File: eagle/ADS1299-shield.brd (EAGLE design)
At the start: 101.6 x 53.3 mm, 133 parts, among them IC1 ADS1299IPAG, IC2 TPS72325DBVT, IC3 TPS73225DBVT, IC5 24AA256UID, IC6 TPS604XXDBV, IC7 OPA376DBV, IC8 OPA376DBV, IC9 TXS0102DCTR, J8 Electrode Connector, U2 TXB0108PWR, U3 TXB0108PWR

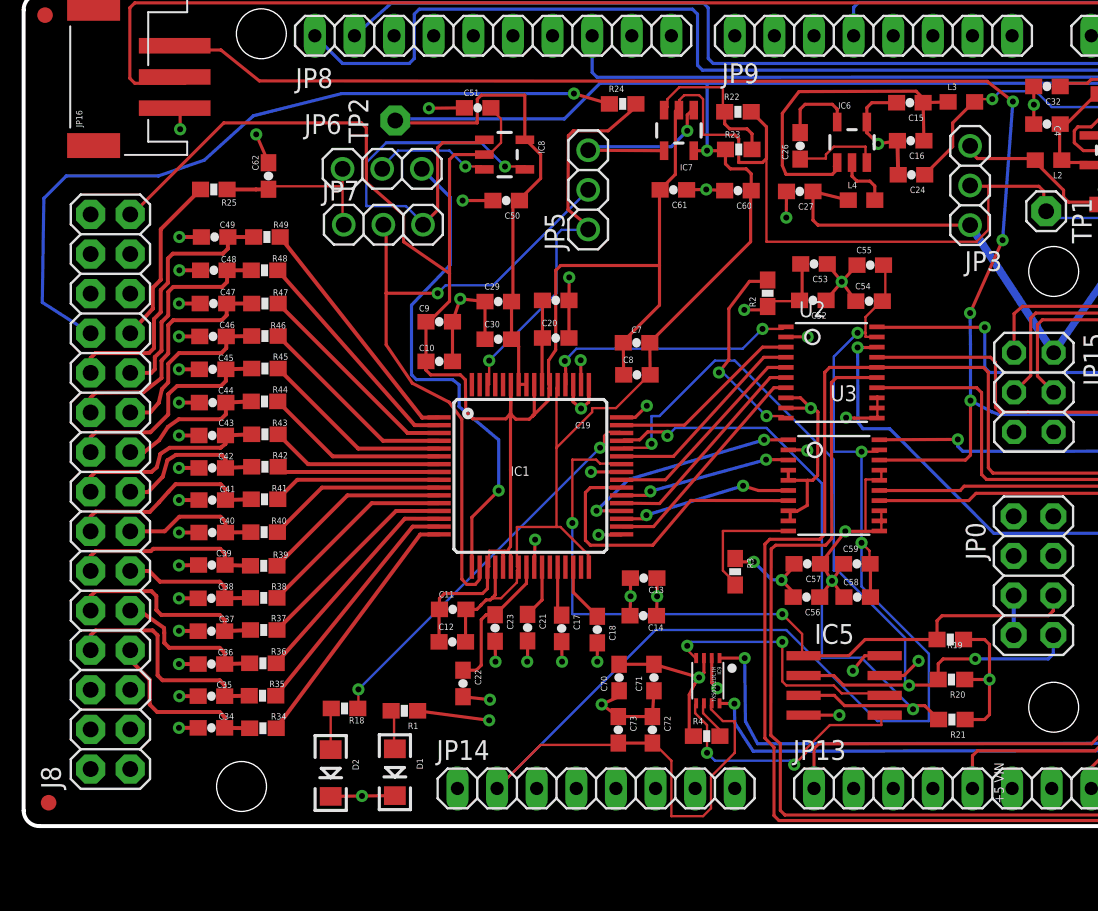
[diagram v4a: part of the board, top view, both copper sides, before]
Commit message: tom side of board is mitered and has polygons on T and V intersections
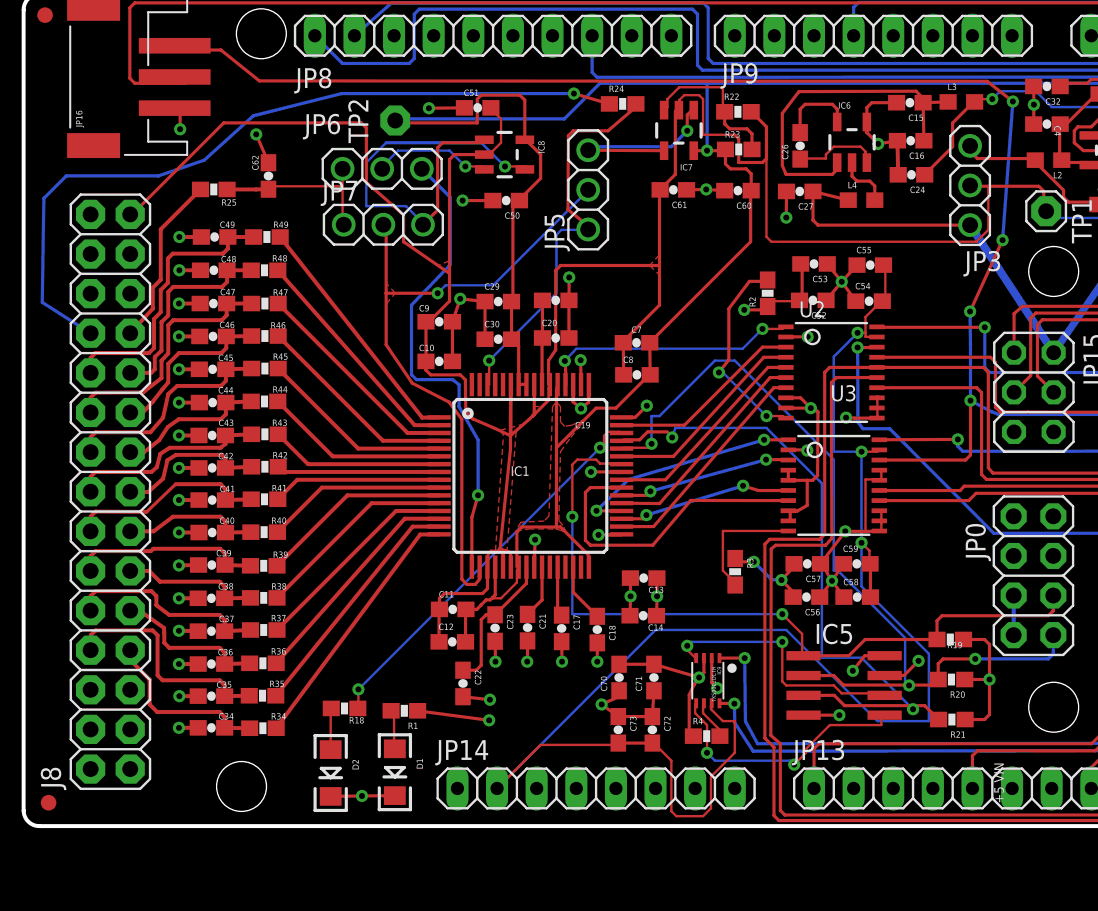
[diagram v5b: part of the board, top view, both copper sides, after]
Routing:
- net AGND: track 466.3 -> 492.9 mm
- net AVDD: track 184.9 -> 188.4 mm
- net SRB2: track 31.8 -> 30.3 mm
- net AVSS: track 163.8 -> 163.2 mm
- added copper zone on layer 1, net AVDD
- added copper zone on layer 1, net AVSS
- added copper zone on layer 1, net SRB1

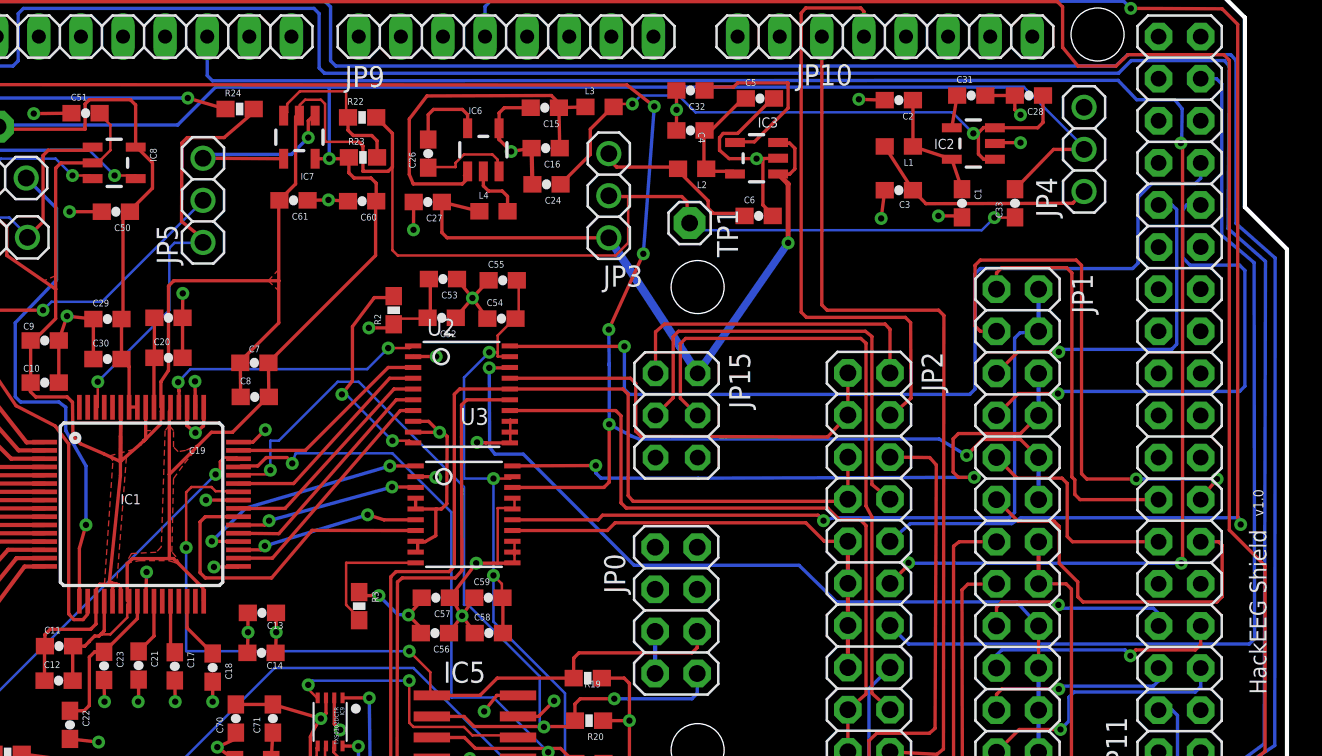
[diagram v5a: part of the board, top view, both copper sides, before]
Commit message: fixed DRC errors related to top-side polygons
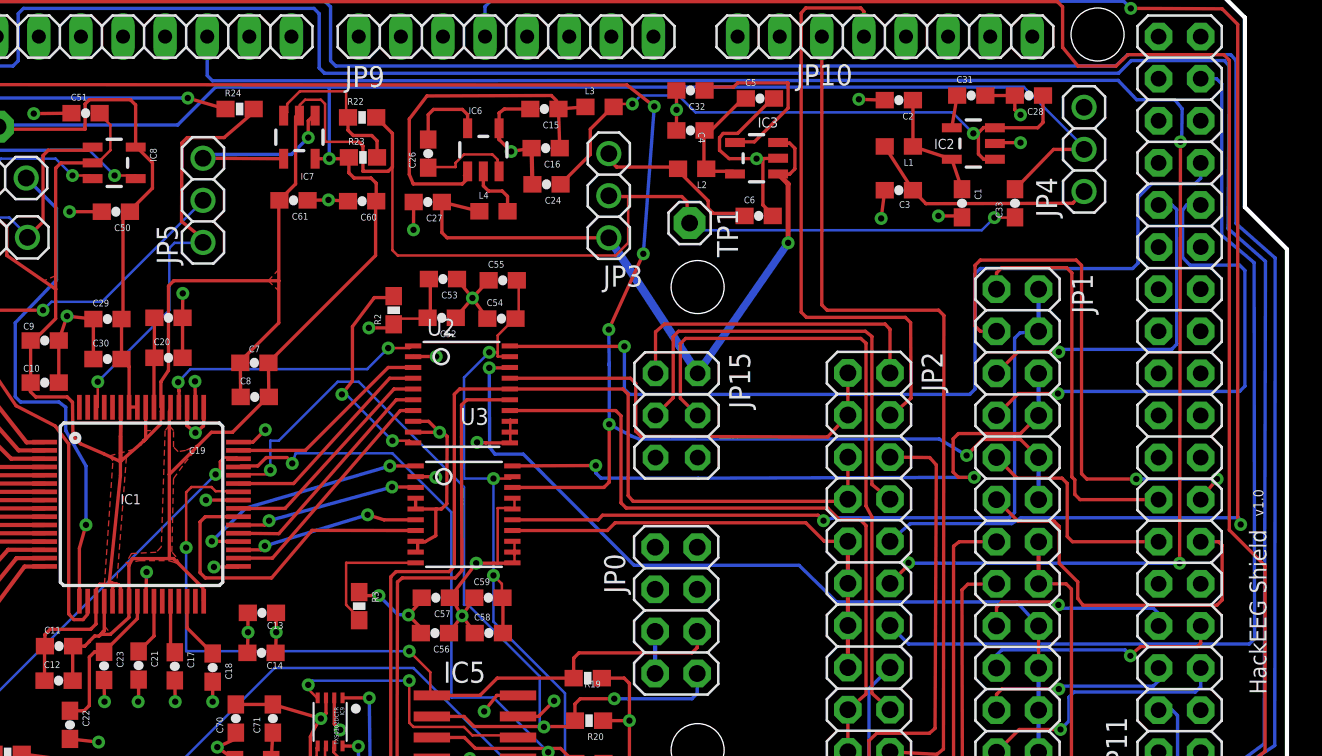
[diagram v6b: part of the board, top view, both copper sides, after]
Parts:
- moved C15 0.08 mm to (56.9, 46.4)
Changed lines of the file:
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@@
 <attribute name="VALUE" x="59.2328" y="45.4152" size="0.4064" layer="27" font="vector"/>
 </element>
-<element name="C15" library="SparkFun-Passives" package="0603-CAP" value="2.2uF" x="56.9468" y="46.5074" smashed="yes" rot="R180">
-<attribute name="NAME" x="57.8358" y="45.7454" size="0.4064" layer="25" font="vector" rot="R180"/>
-<attribute name="VALUE" x="57.9628" y="47.6504" size="0.4064" layer="27" font="vector" rot="R180"/>
+<element name="C15" library="SparkFun-Passives" package="0603-CAP" value="2.2uF" x="56.9214" y="46.4312" smashed="yes" rot="R180">
+<attribute name="NAME" x="57.8104" y="45.6692" size="0.4064" layer="25" font="vector" rot="R180"/>
+<attribute name="VALUE" x="57.9374" y="47.5742" size="0.4064" layer="27" font="vector" rot="R180"/>
 </element>
 <element name="C16" library="SparkFun-Passives" package="0603-CAP" value="10 uF" x="56.9976" y="44.069" smashed="yes" rot="R180">
@@
 <wire x1="80.5434" y1="39.8272" x2="77.2414" y2="39.8272" width="0.2032" layer="2"/>
 <wire x1="54.1884" y1="45.2675" x2="54.1884" y2="46.1899" width="0.2032" layer="1"/>
-<wire x1="54.1884" y1="46.1899" x2="54.5059" y2="46.5074" width="0.2032" layer="1"/>
-<wire x1="54.5059" y1="46.5074" x2="56.0968" y2="46.5074" width="0.2032" layer="1"/>
+<wire x1="54.1884" y1="46.1899" x2="54.5059" y2="46.4312" width="0.2032" layer="1"/>
+<wire x1="54.5059" y1="46.4312" x2="56.0714" y2="46.4312" width="0.2032" layer="1"/>
 <wire x1="55.3304" y1="9.779" x2="56.5658" y2="9.779" width="0.2032" layer="1"/>
 <wire x1="56.5658" y1="9.779" x2="57.5056" y2="10.7188" width="0.2032" layer="1"/>
@@
 <contactref element="C16" pad="1"/>
 <contactref element="IC6" pad="1"/>
-<wire x1="57.7968" y1="46.5074" x2="59.3988" y2="46.5582" width="0.2032" layer="1"/>
-<wire x1="57.7968" y1="46.5074" x2="57.8476" y2="44.069" width="0.2032" layer="1"/>
+<wire x1="57.7714" y1="46.4312" x2="59.3988" y2="46.5582" width="0.2032" layer="1"/>
+<wire x1="57.7714" y1="46.4312" x2="57.8476" y2="44.069" width="0.2032" layer="1"/>
 <wire x1="48.768" y1="45.8216" x2="48.768" y2="42.4815" width="0.2032" layer="1"/>
 <wire x1="48.768" y1="42.4815" x2="49.0093" y2="41.91" width="0.2032" layer="1"/>
@@
 <wire x1="57.3405" y1="47.244" x2="49.8348" y2="47.2186" width="0.2032" layer="1"/>
 <wire x1="52.07" y1="42.418" x2="52.2884" y2="42.6673" width="0.1524" layer="1"/>
-<wire x1="57.658" y1="46.736" x2="57.7968" y2="46.5074" width="0.1524" layer="1"/>
+<wire x1="57.658" y1="46.736" x2="57.7714" y2="46.4312" width="0.1524" layer="1"/>
 <wire x1="51.9709" y1="41.91" x2="52.2884" y2="42.2275" width="0.2032" layer="1"/>
 <wire x1="52.2884" y1="42.2275" x2="52.2884" y2="42.6673" width="0.2032" layer="1"/>
@@
 <contactref element="JP1" pad="14"/>
 <contactref element="JP11" pad="11"/>
-<wire x1="97.8154" y1="20.1041" x2="97.8154" y2="17.0053" width="0.2032" layer="1"/>
-<wire x1="97.8154" y1="17.0053" x2="97.4979" y2="16.6878" width="0.2032" layer="1"/>
-<wire x1="97.4979" y1="16.6878" x2="89.4207" y2="16.6878" width="0.2032" layer="1"/>
-<wire x1="89.4207" y1="16.6878" x2="89.1032" y2="17.0053" width="0.2032" layer="1"/>
-<wire x1="89.1032" y1="17.0053" x2="89.1032" y2="17.8943" width="0.2032" layer="1"/>
+<wire x1="97.8154" y1="20.1041" x2="97.8154" y2="16.8021" width="0.2032" layer="1"/>
+<wire x1="97.8154" y1="16.8021" x2="97.4979" y2="16.4846" width="0.2032" layer="1"/>
+<wire x1="97.4979" y1="16.4846" x2="89.4207" y2="16.4846" width="0.2032" layer="1"/>
+<wire x1="89.4207" y1="16.4846" x2="89.1032" y2="16.9037" width="0.2032" layer="1"/>
+<wire x1="89.1032" y1="16.9037" x2="89.1032" y2="17.8943" width="0.2032" layer="1"/>
 <wire x1="87.9856" y1="21.2471" x2="87.6681" y2="21.5646" width="0.2032" layer="1"/>
 <wire x1="87.6681" y1="21.5646" x2="85.4964" y2="21.5646" width="0.2032" layer="1"/>
@@
 <contactref element="JP1" pad="6"/>
 <contactref element="JP11" pad="7"/>
-<wire x1="96.52" y1="15.24" x2="96.52" y2="14.1097" width="0.2032" layer="1"/>
-<wire x1="96.52" y1="14.1097" x2="96.2025" y2="13.7922" width="0.2032" layer="1"/>
-<wire x1="96.2025" y1="13.7922" x2="92.5957" y2="13.7922" width="0.2032" layer="1"/>
-<wire x1="92.5957" y1="13.7922" x2="92.2782" y2="13.4747" width="0.2032" layer="1"/>
+<wire x1="96.52" y1="15.24" x2="96.52" y2="14.2113" width="0.2032" layer="1"/>
+<wire x1="96.52" y1="14.2113" x2="96.3041" y2="13.9954" width="0.2032" layer="1"/>
+<wire x1="96.3041" y1="13.9954" x2="92.9005" y2="13.9954" width="0.2032" layer="1"/>
+<wire x1="92.9005" y1="13.9954" x2="92.2782" y2="13.4747" width="0.2032" layer="1"/>
 <wire x1="92.2782" y1="13.4747" x2="92.2782" y2="13.4366" width="0.2032" layer="1"/>
 <via x="92.2782" y="13.4366" extent="1-16" drill="0.381"/>
@@
 <wire x1="94.9579" y1="46.99" x2="95.4024" y2="46.4439" width="0.2032" layer="16"/>
 <wire x1="95.4024" y1="46.4439" x2="95.377" y2="44.6532" width="0.2032" layer="16"/>
-<wire x1="95.377" y1="44.6532" x2="95.3262" y2="44.3738" width="0.2032" layer="16"/>
-<via x="95.3262" y="44.3738" extent="1-16" drill="0.381"/>
-<wire x1="95.3262" y1="44.3738" x2="95.4278" y2="44.069" width="0.2032" layer="1"/>
-<wire x1="95.4278" y1="44.069" x2="95.4278" y2="19.2278" width="0.2032" layer="1"/>
-<wire x1="95.4278" y1="19.2278" x2="95.3516" y2="19.0246" width="0.2032" layer="1"/>
-<via x="95.3516" y="19.0246" extent="1-16" drill="0.381"/>
-<wire x1="95.3516" y1="19.0246" x2="78.9178" y2="19.0246" width="0.2032" layer="16"/>
+<wire x1="95.377" y1="44.6532" x2="95.3008" y2="44.45" width="0.2032" layer="16"/>
+<via x="95.3008" y="44.45" extent="1-16" drill="0.381"/>
+<wire x1="95.3008" y1="44.45" x2="95.3008" y2="44.1198" width="0.2032" layer="1"/>
+<wire x1="95.3008" y1="44.1198" x2="95.25" y2="19.2532" width="0.2032" layer="1"/>
+<wire x1="95.25" y1="19.2532" x2="95.25" y2="19.0246" width="0.2032" layer="1"/>
+<via x="95.25" y="19.0246" extent="1-16" drill="0.381"/>
+<wire x1="95.25" y1="19.0246" x2="78.9178" y2="19.0246" width="0.2032" layer="16"/>
 <wire x1="78.9178" y1="19.0246" x2="78.8924" y2="19.05" width="0.2032" layer="16"/>
 <via x="78.8924" y="19.05" extent="1-16" drill="0.381"/>
@@
 <wire x1="40.386" y1="31.242" x2="40.2708" y2="31.115" width="0.1524" layer="1"/>
 <wire x1="46.736" y1="40.64" x2="46.7732" y2="40.8686" width="0.1524" layer="1"/>
-<wire x1="31.75" y1="15.748" x2="31.75" y2="16.51" width="0.1524" layer="1"/>
-<wire x1="30.734" y1="14.732" x2="31.75" y2="15.748" width="0.1524" layer="1"/>
-<wire x1="30.226" y1="14.732" x2="30.734" y2="14.732" width="0.1524" layer="1"/>
-<wire x1="31.75" y1="16.51" x2="31.8636" y2="16.7306" width="0.1524" layer="1"/>
+<wire x1="31.8516" y1="15.748" x2="31.8516" y2="16.51" width="0.2032" layer="1"/>
+<wire x1="30.734" y1="14.732" x2="31.8516" y2="15.748" width="0.2032" layer="1"/>
+<wire x1="30.226" y1="14.732" x2="30.734" y2="14.732" width="0.2032" layer="1"/>
+<wire x1="31.8516" y1="16.51" x2="31.8636" y2="16.7306" width="0.1524" layer="1"/>
 <wire x1="30.226" y1="14.732" x2="30.18685" y2="14.77115" width="0.1524" layer="1"/>
 <wire x1="36.322" y1="17.526" x2="36.322" y2="16.764" width="0.1524" layer="1"/>
 <wire x1="34.544" y1="19.304" x2="36.322" y2="17.526" width="0.2032" layer="1"/>
-<wire x1="31.75" y1="16.764" x2="31.75" y2="18.9865" width="0.2032" layer="1"/>
-<wire x1="31.75" y1="18.9865" x2="32.0675" y2="19.304" width="0.2032" layer="1"/>
+<wire x1="31.8516" y1="16.764" x2="31.8516" y2="18.8849" width="0.2032" layer="1"/>
+<wire x1="31.8516" y1="18.8849" x2="32.0675" y2="19.304" width="0.2032" layer="1"/>
 <wire x1="32.0675" y1="19.304" x2="34.29" y2="19.304" width="0.2032" layer="1"/>
 <wire x1="34.29" y1="19.304" x2="34.544" y2="19.304" width="0.2032" layer="1"/>
 <wire x1="36.322" y1="16.764" x2="36.3636" y2="16.7306" width="0.1524" layer="1"/>
-<wire x1="31.75" y1="16.764" x2="31.8636" y2="16.7306" width="0.1524" layer="1"/>
+<wire x1="31.8516" y1="16.764" x2="31.8636" y2="16.7306" width="0.1524" layer="1"/>
 <wire x1="34.29" y1="19.304" x2="34.29" y2="24.384" width="0.2032" layer="1"/>
 <wire x1="34.29" y1="24.384" x2="34.29" y2="28.194" width="0.2032" layer="1"/>
@@
 <vertex x="34.29" y="27.3304"/>
 </polygon>
-</signal>
+<polygon width="0.0254" layer="1">
+<vertex x="30.3784" y="15.24"/>
+<vertex x="30.7848" y="14.732"/>
+<vertex x="30.0736" y="14.6304"/>
+</polygon>
+</signal>

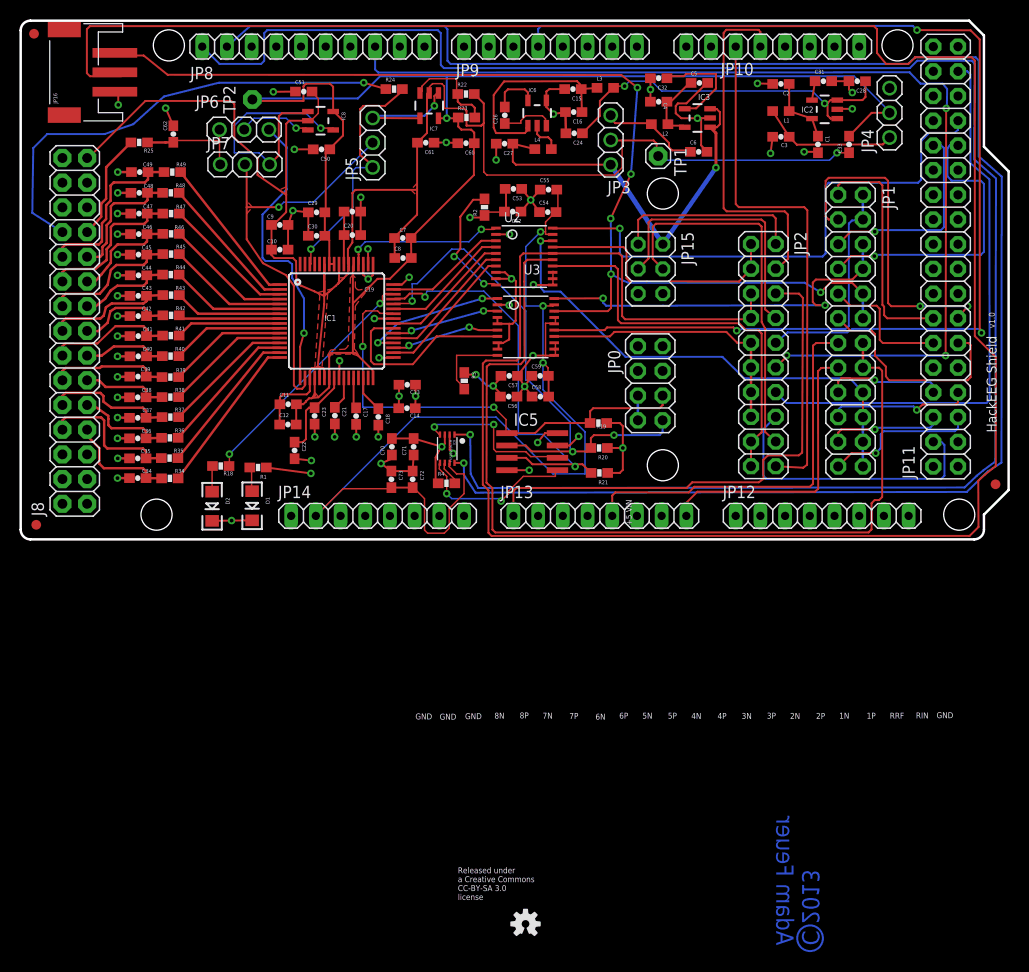
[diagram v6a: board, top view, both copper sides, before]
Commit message: supply polygons for AVDD and AVSS under the ADS1299; more tuning and mitering on top and bottom
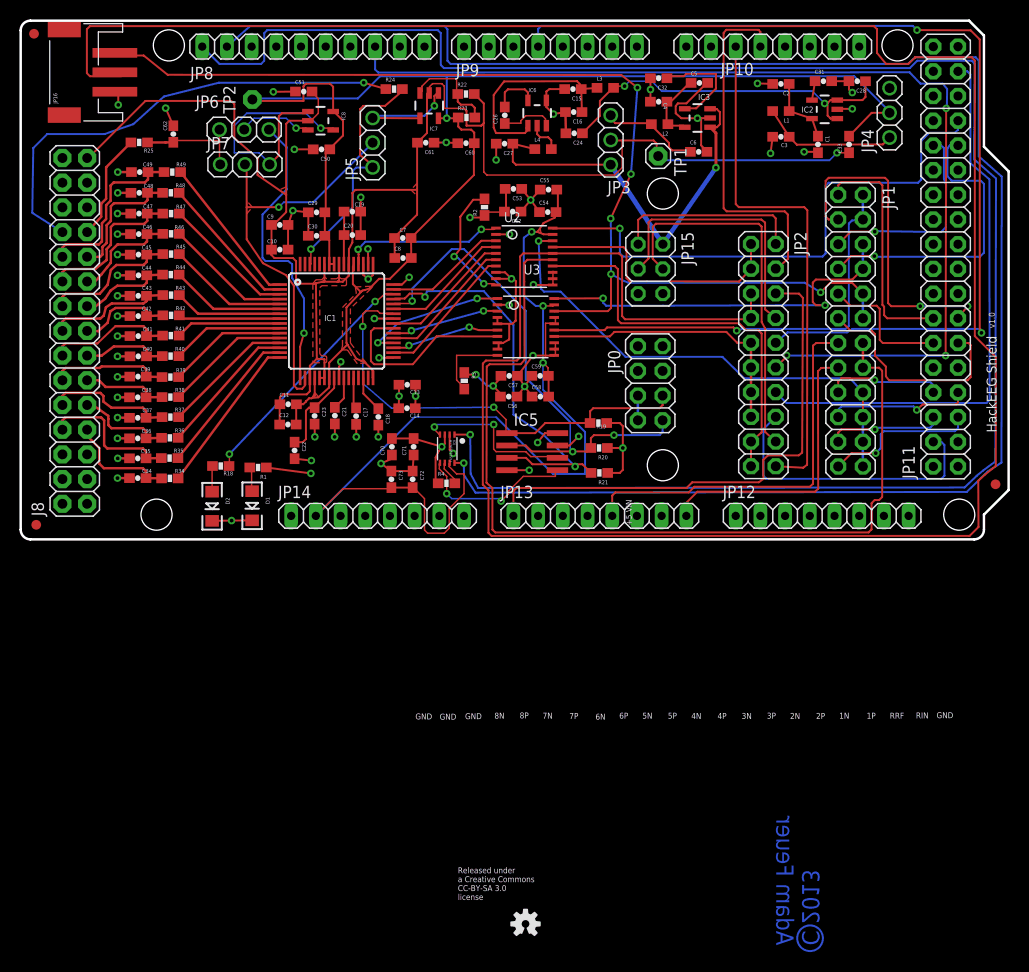
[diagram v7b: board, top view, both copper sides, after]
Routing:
- net AVDD: track 188.4 -> 182.1 mm
- net BOARD_ADDR_0: track 48.6 -> 47.1 mm
- net BOARD_ADDR_2: track 43.1 -> 41.9 mm
- net AVSS: track 163.1 -> 162.4 mm
- net IOREF: track 102.3 -> 102.8 mm
- added copper zone on layer 1, net IOREF
